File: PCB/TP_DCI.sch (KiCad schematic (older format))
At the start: 70 parts, among them J8 Molex_KK254, J9 Molex_KK254, K1 G5V-1, K2 G5V-1, P1 Conn_Poncho2P_2x_20x2, Q1 BC817W, Q2 BC817W, U1 PS2805-4, U2 ACS725xLCTR-10AU, U3 ACS725xLCTR-10AU, U4 DS3231, U5 24AA1025

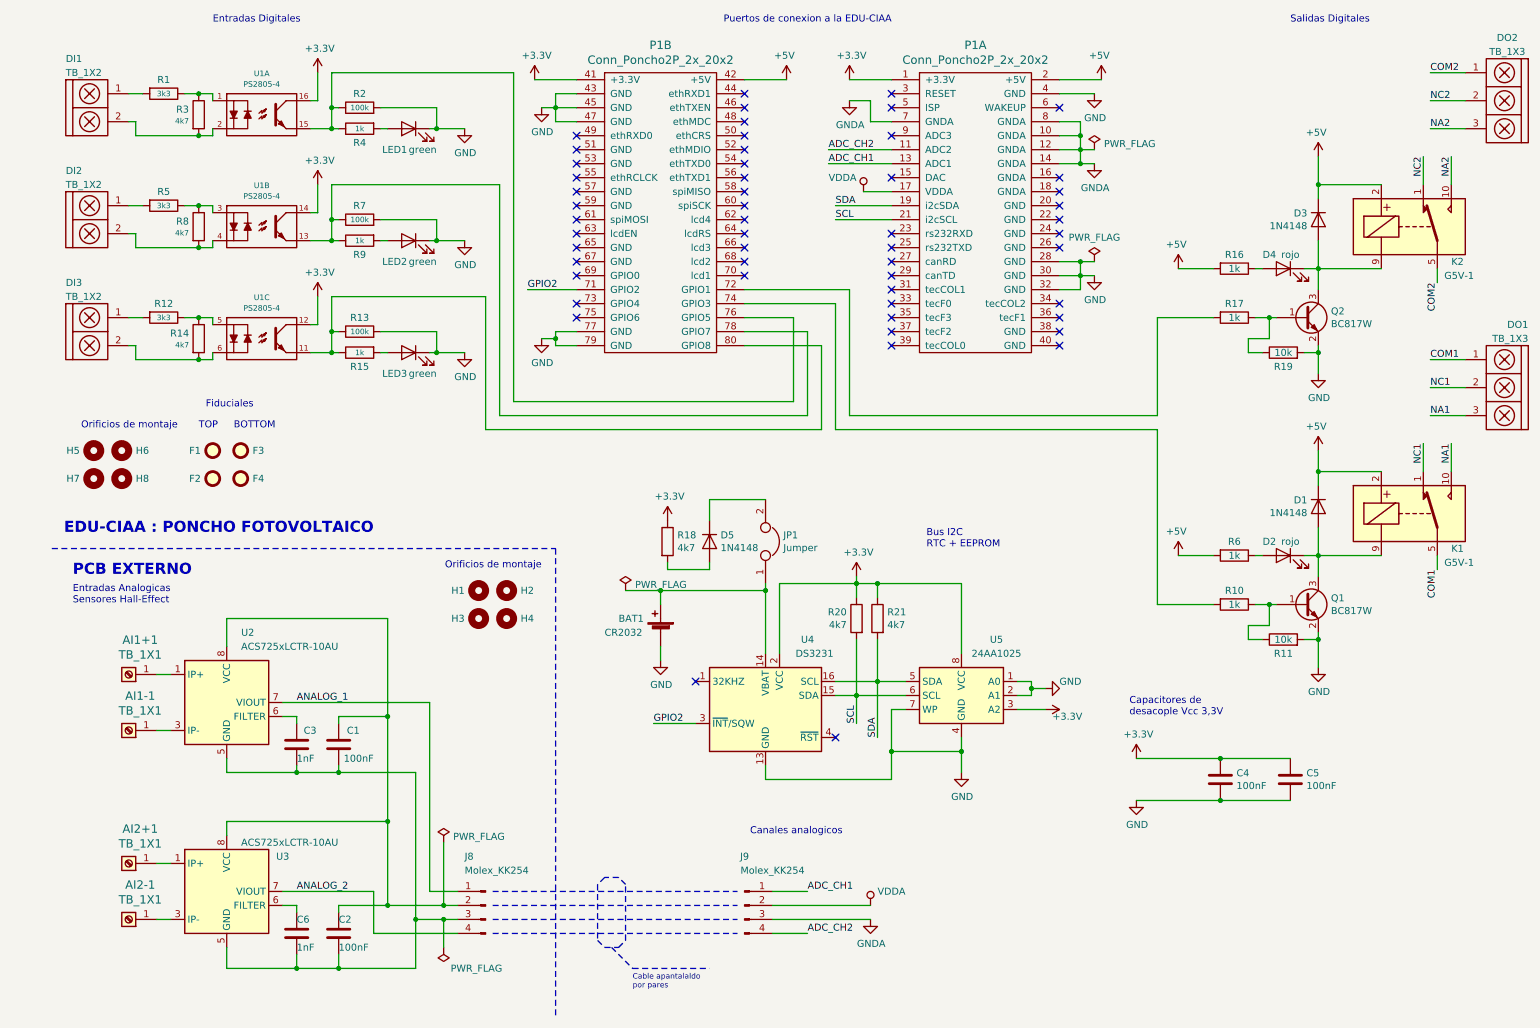
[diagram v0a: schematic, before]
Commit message: Correcciones segun sugerencias del docente
- se incremento el ancho de tracks, tamaño de vias y clearance.
- el tamaño amplio del poncho se justifica por cuestiones mecánicas, para lograr mas puntos de anclaje a la EDU-CIAA
- se agregan comentarios para el fabricante.
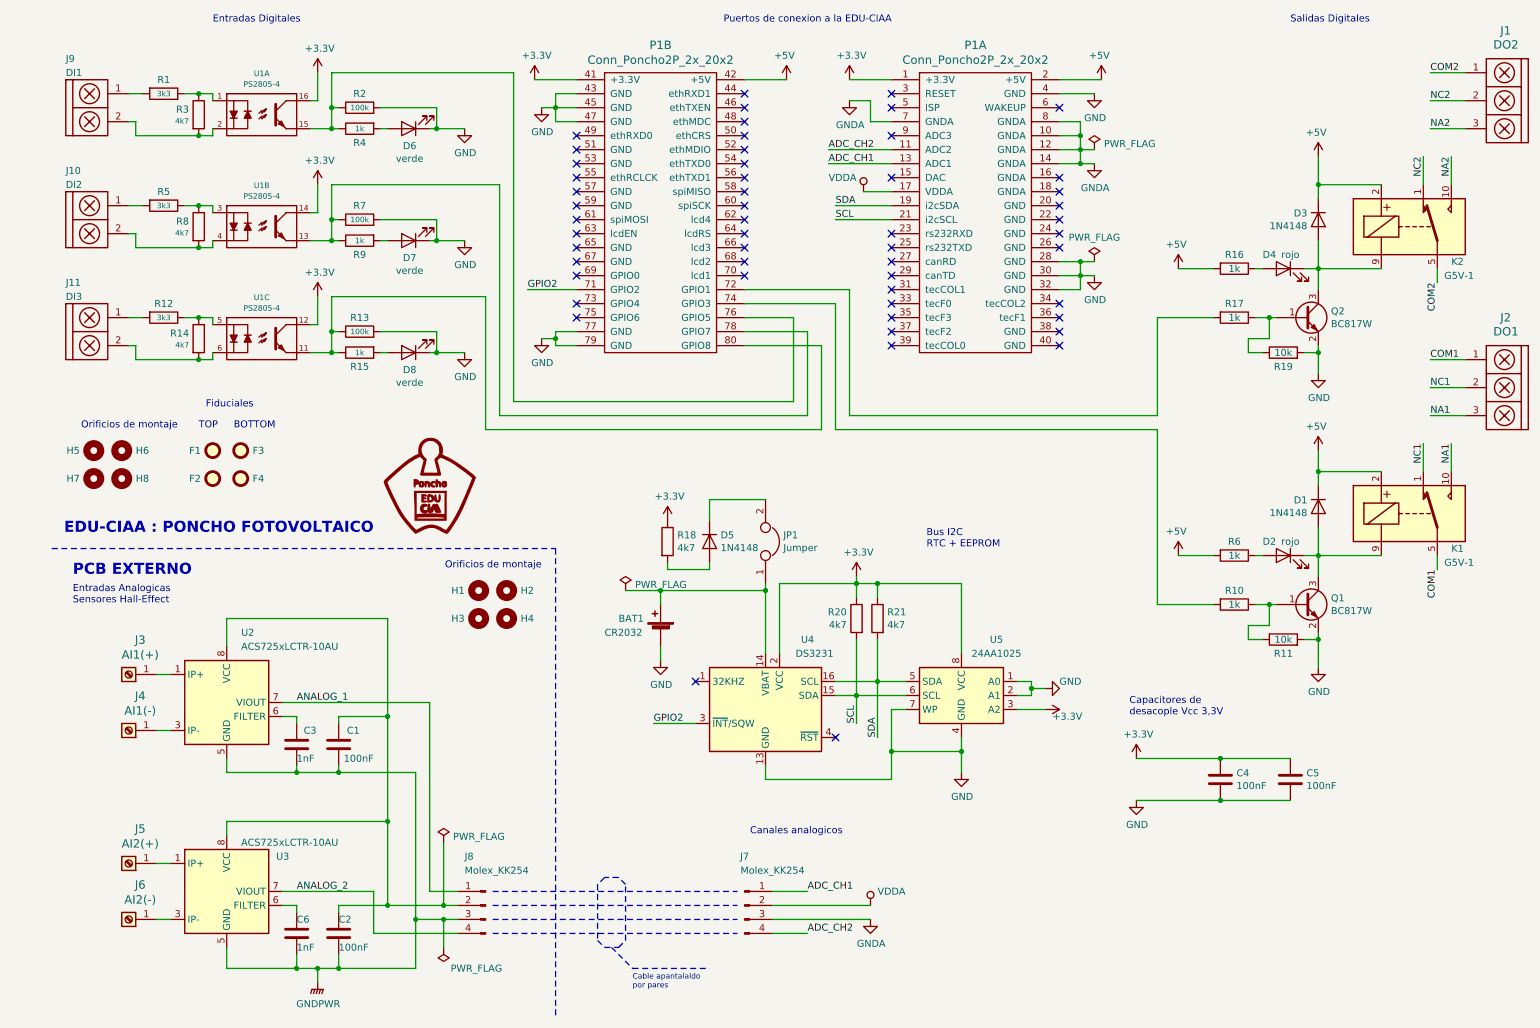
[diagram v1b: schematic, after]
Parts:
- removed DO1, DO2: TB_1X3, Libreria_EDU_CIAA_NXP:bornier3, symbol w_device:TB_1X3
- removed LED1, LED2, LED3: green, LED_SMD:LED_0805_2012Metric, symbol Device:LED
- added D6, D7, D8: verde, LED_SMD:LED_0805_2012Metric, symbol Device:LED
- added G1: Logo_Poncho, Poncho_Esqueleto:Logo_Poncho, symbol Poncho_Esqueleto:Logo_Poncho
- added J1: DO2, Libreria_EDU_CIAA_NXP:bornier3, symbol w_device:TB_1X3
- added J2: DO1, Libreria_EDU_CIAA_NXP:bornier3, symbol w_device:TB_1X3
- J10: renamed from DI2; value TB_1X2 -> DI2
- J11: renamed from DI3; value TB_1X2 -> DI3
- J3: renamed from AI1+1; value TB_1X1 -> AI1(+)
- J4: renamed from AI1-1; value TB_1X1 -> AI1(-)
- J5: renamed from AI2+1; value TB_1X1 -> AI2(+)
- J6: renamed from AI2-1; value TB_1X1 -> AI2(-)
- J9: renamed from DI1; value TB_1X2 -> DI1
- K1, K2: Codigo Digikey (none) -> Z773-ND
- U1: Codigo Digikey (none) -> PS2805-4A-ND
- renumbered J9 to J7
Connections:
- net COM1: now also J2.1
- net COM2: now also J1.1
- net GND: now also D6.1 (K), D7.1 (K), D8.1 (K)
- net NA1: now also J2.3
- net NA2: now also J1.3
- net NC1: now also J2.2
- net NC2: now also J1.2
- net GNDPWR: now reaches C1.2, C2.2, C3.2, C6.2, J8.3 (Pin_3), U2.5 (GND), U3.5 (GND)
- net at R4.2: now also D6.2 (A)
- net at R9.2: now also D7.2 (A)
- net at R15.2: now also D8.2 (A)
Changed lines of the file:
@@
 Canales analogicos
 $Comp
-L Connector:Conn_01x04_Male J9
+L Connector:Conn_01x04_Male J7
 U 1 1 5EED22B4
 P 5450 7000
-F 0 "J9" H 5450 7350 50  0000 C CNN
+F 0 "J7" H 5450 7350 50  0000 C CNN
 F 1 "Molex_KK254" H 5650 7250 50  0000 C CNN
 F 2 "Connector_Molex:Molex_KK-254_AE-6410-04A_1x04_P2.54mm_Vertical" H 5450 7000 50  0001 C CNN
@@
 $EndComp
 $Comp
-L Connector:Screw_Terminal_01x01 AI1+1
+L Connector:Screw_Terminal_01x01 J3
 U 1 1 5EEA00D2
 P 1050 5350
-F 0 "AI1+1" H 968 5103 60  0000 C CNN
-F 1 "TB_1X1" H 968 5209 60  0000 C CNN
+F 0 "J3" H 968 5103 60  0000 C CNN
+F 1 "AI1(+)" H 968 5209 60  0000 C CNN
 F 2 "CIAA_footprints:wurth_connector" H 1182 5633 60  0001 C CNN
 F 3 "" H 1000 5400 60  0000 C CNN
@@
 Text Label 10350 3500 0    50   ~ 0
 NA1
-$Comp
-L w_device:TB_1X3 DO1
-U 1 1 5EE96028
-P 10950 3200
-F 0 "DO1" H 10850 3550 50  0000 L CNN
-F 1 "TB_1X3" H 10850 3450 50  0000 L CNN
-F 2 "Libreria_EDU_CIAA_NXP:bornier3" H 11082 3483 60  0001 C CNN
-F 3 "" H 10900 3250 60  0000 C CNN
-	1    10950 3200
-	-1   0    0    -1
-$EndComp
 Wire Wire Line
 	10600 3100 10350 3100
@@
 	0    -1   -1   0
 $EndComp
-$Comp
-L w_device:TB_1X3 DO2
-U 1 1 5F144B65
-P 10950 1150
-F 0 "DO2" H 11000 1500 50  0000 C CNN
-F 1 "TB_1X3" H 11000 1400 50  0000 C CNN
-F 2 "Libreria_EDU_CIAA_NXP:bornier3" H 11082 1433 60  0001 C CNN
-F 3 "" H 10900 1200 60  0000 C CNN
-	1    10950 1150
-	-1   0    0    -1
-$EndComp
 Wire Wire Line
 	10400 2550 10400 2450
@@
 Connection ~ 2250 7450
 Wire Wire Line
-	2250 7450 2550 7450
+	2250 7450 2400 7450
 Connection ~ 2550 7450
 Connection ~ 2900 6400
@@
 F 2 "Relay_THT:Relay_SPDT_Omron_G5V-1" H 11330 2120 50  0001 C CNN
 F 3 "http://omronfs.omron.com/en_US/ecb/products/pdf/en-g5v_1.pdf" H 10200 2150 50  0001 C CNN
+F 4 "Z773-ND" H 10200 2150 50  0001 C CNN "Codigo Digikey"
 	1    10200 2150
 	1    0    0    -1
@@
 F 2 "Relay_THT:Relay_SPDT_Omron_G5V-1" H 11330 4170 50  0001 C CNN
 F 3 "http://omronfs.omron.com/en_US/ecb/products/pdf/en-g5v_1.pdf" H 10200 4200 50  0001 C CNN
+F 4 "Z773-ND" H 10200 4200 50  0001 C CNN "Codigo Digikey"
 	1    10200 4200
 	1    0    0    -1
@@
 	5600 6100 6500 6100
 $Comp
-L Connector:Screw_Terminal_01x01 AI1-1
+L Connector:Screw_Terminal_01x01 J4
 U 1 1 5EDE1FB3
 P 1050 5750
-F 0 "AI1-1" H 968 5503 60  0000 C CNN
-F 1 "TB_1X1" H 968 5609 60  0000 C CNN
+F 0 "J4" H 968 5503 60  0000 C CNN
+F 1 "AI1(-)" H 968 5609 60  0000 C CNN
 F 2 "CIAA_footprints:wurth_connector" H 1182 6033 60  0001 C CNN
 F 3 "" H 1000 5800 60  0000 C CNN
@@
 	1250 6700 1350 6700
 $Comp
-L Connector:Screw_Terminal_01x01 AI2+1
+L Connector:Screw_Terminal_01x01 J5
 U 1 1 5EE2CC55
 P 1050 6700
-F 0 "AI2+1" H 968 6453 60  0000 C CNN
-F 1 "TB_1X1" H 968 6559 60  0000 C CNN
+F 0 "J5" H 968 6453 60  0000 C CNN
+F 1 "AI2(+)" H 968 6559 60  0000 C CNN
 F 2 "CIAA_footprints:wurth_connector" H 1182 6983 60  0001 C CNN
 F 3 "" H 1000 6750 60  0000 C CNN
@@
 $EndComp
 $Comp
-L Connector:Screw_Terminal_01x01 AI2-1
+L Connector:Screw_Terminal_01x01 J6
 U 1 1 5EE2CC5F
 P 1050 7100
-F 0 "AI2-1" H 968 6853 60  0000 C CNN
-F 1 "TB_1X1" H 968 6959 60  0000 C CNN
+F 0 "J6" H 968 6853 60  0000 C CNN
+F 1 "AI2(-)" H 968 6959 60  0000 C CNN
 F 2 "CIAA_footprints:wurth_connector" H 1182 7383 60  0001 C CNN
 F 3 "" H 1000 7150 60  0000 C CNN
@@
 F 1 "PS2805-4" H 2000 1568 40  0000 C CNN
 F 2 "Package_SO:SOP-16_4.4x10.4mm_P1.27mm" H 1836 1176 29  0001 C CNN
-F 3 "" H 2000 1350 60  0000 C CNN
+F 3 "http://www.cel.com/pdf/datasheets/ps2805.pdf" H 2000 1350 60  0001 C CNN
+F 4 "PS2805-4A-ND" H 2000 1350 50  0001 C CNN "Codigo Digikey"
 	1    2000 1350
 	1    0    0    -1
@@
 	2850 1450 2900 1450
 $Comp
-L Device:LED LED1
-U 1 1 5F79458B
-P 3050 1450
-F 0 "LED1" H 3150 1300 50  0000 C CNN
-F 1 "green" H 2950 1300 50  0000 C CNN
-F 2 "LED_SMD:LED_0805_2012Metric" H 3050 1450 50  0001 C CNN
-F 3 "~" H 3050 1450 50  0001 C CNN
-	1    3050 1450
-	-1   0    0    -1
-$EndComp
-$Comp
 L Device:R R2
 U 1 1 5F76DBB2
@@
 F 1 "PS2805-4" H 2000 2368 40  0000 C CNN
 F 2 "Package_SO:SOP-16_4.4x10.4mm_P1.27mm" H 1836 1976 29  0001 C CNN
-F 3 "" H 2000 2150 60  0000 C CNN
+F 3 "http://www.cel.com/pdf/datasheets/ps2805.pdf" H 2000 2150 60  0001 C CNN
 F 4 "PS2805-4A-ND" H 2000 2150 50  0001 C CNN "Codigo Digikey"
 	2    2000 2150
@@
 Wire Wire Line
 	2850 2250 2900 2250
-$Comp
-L Device:LED LED2
-U 1 1 605559D3
-P 3050 2250
-F 0 "LED2" H 3150 2100 50  0000 C CNN
-F 1 "green" H 2950 2100 50  0000 C CNN
-F 2 "LED_SMD:LED_0805_2012Metric" H 3050 2250 50  0001 C CNN
-F 3 "~" H 3050 2250 50  0001 C CNN
-	1    3050 2250
-	-1   0    0    -1
-$EndComp
 $Comp
 L Device:R R7
@@
 Wire Wire Line
 	2850 3050 2900 3050
-$Comp
-L Device:LED LED3
-U 1 1 6066CF61
-P 3050 3050
-F 0 "LED3" H 3150 2900 50  0000 C CNN
-F 1 "green" H 2950 2900 50  0000 C CNN
-F 2 "LED_SMD:LED_0805_2012Metric" H 3050 3050 50  0001 C CNN
-F 3 "~" H 3050 3050 50  0001 C CNN
-	1    3050 3050
-	-1   0    0    -1
-$EndComp
 $Comp
 L Device:R R13
@@
 	4250 1200 4100 1200
 Wire Wire Line
-	2500 1050 3800 1050
-Wire Wire Line
 	2500 1850 3700 1850
 Wire Wire Line
@@
 $EndComp
 $Comp
-L w_device:TB_1X2 DI2
+L w_device:TB_1X2 J10
 U 1 1 5F26CDA1
 P 700 2100
-F 0 "DI2" H 600 2450 50  0000 L CNN
-F 1 "TB_1X2" H 600 2350 50  0000 L CNN
+F 0 "J10" H 600 2450 50  0000 L CNN
+F 1 "DI2" H 600 2350 50  0000 L CNN
 F 2 "Libreria_EDU_CIAA_NXP:bornier2" H 832 2383 60  0001 C CNN
 F 3 "" H 650 2150 60  0000 C CNN
@@
 F 1 "PS2805-4" H 2000 3168 40  0000 C CNN
 F 2 "Package_SO:SOP-16_4.4x10.4mm_P1.27mm" H 1836 2776 29  0001 C CNN
-F 3 "" H 2000 2950 60  0000 C CNN
+F 3 "http://www.cel.com/pdf/datasheets/ps2805.pdf" H 2000 2950 60  0001 C CNN
+F 4 "PS2805-4A-ND" H 2000 2950 50  0001 C CNN "Codigo Digikey"
 	3    2000 2950
 	1    0    0    -1
 $EndComp
 $Comp
-L w_device:TB_1X2 DI1
+L w_device:TB_1X2 J9
 U 1 1 5EF8CDE6
 P 700 1300
-F 0 "DI1" H 600 1650 50  0000 L CNN
-F 1 "TB_1X2" H 600 1550 50  0000 L CNN
+F 0 "J9" H 600 1650 50  0000 L CNN
+F 1 "DI1" H 600 1550 50  0000 L CNN
 F 2 "Libreria_EDU_CIAA_NXP:bornier2" H 832 1583 60  0001 C CNN
 F 3 "" H 650 1350 60  0000 C CNN
@@
 $EndComp
 $Comp
-L w_device:TB_1X2 DI3
+L w_device:TB_1X2 J11
 U 1 1 5F491F3E
 P 700 2900
-F 0 "DI3" H 600 3250 50  0000 L CNN
-F 1 "TB_1X2" H 600 3150 50  0000 L CNN
+F 0 "J11" H 600 3250 50  0000 L CNN
+F 1 "DI3" H 600 3150 50  0000 L CNN
 F 2 "Libreria_EDU_CIAA_NXP:bornier2" H 832 3183 60  0001 C CNN
 F 3 "" H 650 2950 60  0000 C CNN
@@
 Wire Wire Line
 	6000 3000 6000 3600
+$Comp
+L Device:LED D6
+U 1 1 5F0C1433
+P 3050 1450
+F 0 "D6" H 3043 1573 50  0000 C CNN
+F 1 "verde" H 3043 1664 50  0000 C CNN
+F 2 "LED_SMD:LED_0805_2012Metric" H 3050 1450 50  0001 C CNN
+F 3 "~" H 3050 1450 50  0001 C CNN
+	1    3050 1450
+	-1   0    0    1
+$EndComp
+Wire Wire Line
+	2500 1050 3800 1050
+$Comp
+L Device:LED D7
+U 1 1 5F0FB0B5
+P 3050 2250
+F 0 "D7" H 3043 2373 50  0000 C CNN
+F 1 "verde" H 3043 2464 50  0000 C CNN
+F 2 "LED_SMD:LED_0805_2012Metric" H 3050 2250 50  0001 C CNN
+F 3 "~" H 3050 2250 50  0001 C CNN
+	1    3050 2250
+	-1   0    0    1
+$EndComp
+$Comp
+L Device:LED D8
+U 1 1 5F0FB94C
+P 3050 3050
+F 0 "D8" H 3043 3173 50  0000 C CNN
+F 1 "verde" H 3043 3264 50  0000 C CNN
+F 2 "LED_SMD:LED_0805_2012Metric" H 3050 3050 50  0001 C CNN
+F 3 "~" H 3050 3050 50  0001 C CNN
+	1    3050 3050
+	-1   0    0    1
+$EndComp
+$Comp
+L w_device:TB_1X3 J1
+U 1 1 5F12E750
+P 10950 1150
+F 0 "J1" H 11050 1550 60  0000 R CNN
+F 1 "DO2" H 11100 1450 60  0000 R CNN
+F 2 "Libreria_EDU_CIAA_NXP:bornier3" H 10900 1200 60  0001 C CNN
+F 3 "" H 10900 1200 60  0000 C CNN
+	1    10950 1150
+	-1   0    0    -1
+$EndComp
+$Comp
+L w_device:TB_1X3 J2
+U 1 1 5F170413
+P 10950 3200
+F 0 "J2" H 11050 3600 60  0000 R CNN
+F 1 "DO1" H 11100 3500 60  0000 R CNN
+F 2 "Libreria_EDU_CIAA_NXP:bornier3" H 10900 3250 60  0001 C CNN
+F 3 "" H 10900 3250 60  0000 C CNN
+	1    10950 3200
+	-1   0    0    -1
+$EndComp
+$Comp
+L power:GNDPWR #PWR0134
+U 1 1 5F2065A8
+P 2400 7550
+F 0 "#PWR0134" H 2400 7350 50  0001 C CNN
+F 1 "GNDPWR" H 2404 7396 50  0000 C CNN
+F 2 "" H 2400 7500 50  0001 C CNN
+F 3 "" H 2400 7500 50  0001 C CNN
+	1    2400 7550
+	1    0    0    -1
+$EndComp
+Wire Wire Line
+	2400 7550 2400 7450
+Connection ~ 2400 7450
+Wire Wire Line
+	2400 7450 2550 7450
+$Comp
+L Poncho_Esqueleto:Logo_Poncho G1
+U 1 1 5F4C540D
+P 3200 4000
+F 0 "G1" H 3150 3600 60  0001 C CNN
+F 1 "Logo_Poncho" H 3400 3600 60  0001 C CNN
+F 2 "Poncho_Esqueleto:Logo_Poncho" H 3200 4416 60  0001 C CNN
+F 3 "" H 3200 4000 60  0001 C CNN
+	1    3200 4000
+	1    0    0    -1
+$EndComp
 $EndSCHEMATC
